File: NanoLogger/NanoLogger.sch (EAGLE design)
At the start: 18 parts, among them IC1 TINY11S, U4 LIS331, X1 USB-MICROB

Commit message: Lots of fixes, added NanoLogger
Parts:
- removed BAT1: (no value), SparkFun:BATTERY20SMD
- removed JP2: (no value), SparkFun:M061X06-SMD_EDGE_FEMALE
- removed R1, R2: 68, SparkFun:RESISTOR0402-RES
- removed R4: 1.5k, SparkFun:RESISTOR0402-RES
- removed R7: 4.7k, SparkFun:RESISTOR0402-RES
- removed X1: USB-MICROB, SparkFun:USB-MICROB
- added BAT2: (no value), SparkFun:BATTERY12MM
- added CS, GND, MISO, MOSI, SCK, VCC: TPTP08R, testpad:TPTP08R
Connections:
- removed net N$13: IC1.(XTAL2)PB4, R1.1, R6.2
- removed net N$2: R2.2, X1.D+
- removed net N$8: R1.2, R4.1, X1.D-
- removed net N$9: IC1.(RESET)PB5, R7.1
- new net N$11: IC1.(XTAL2)PB4, U4.CS
- new net N$12: CS.TP, IC1.(RESET)PB5, R6.2, U4.INT1
- net GND: now also BAT2.-, GND.TP; no longer BAT1.-, JP2.5, X1.GND
- net N$4: no longer JP2.4, R2.1, U4.CS
- net N$5: now also SCK.TP; no longer JP2.3
- net N$6: now also MOSI.TP; no longer JP2.1, U4.INT1
- net N$7: now also MISO.TP; no longer JP2.2
- net VCC: now also BAT2.+, VCC.TP; no longer BAT1.+, JP2.6, R4.2, R7.2
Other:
- note added: "NanoLogger"
- note removed: "CoinLogger"
- note removed: "If it's an input, we can look for the accel interrupt for ultra low power mode."
- note removed: "It's also CS, so by default, the accel is selected, but Flash can also be selected if CS is driven low."
- note removed: "PB4: LED is on by default since that line is pulled up because of USB"
- moved on the sheet: R6

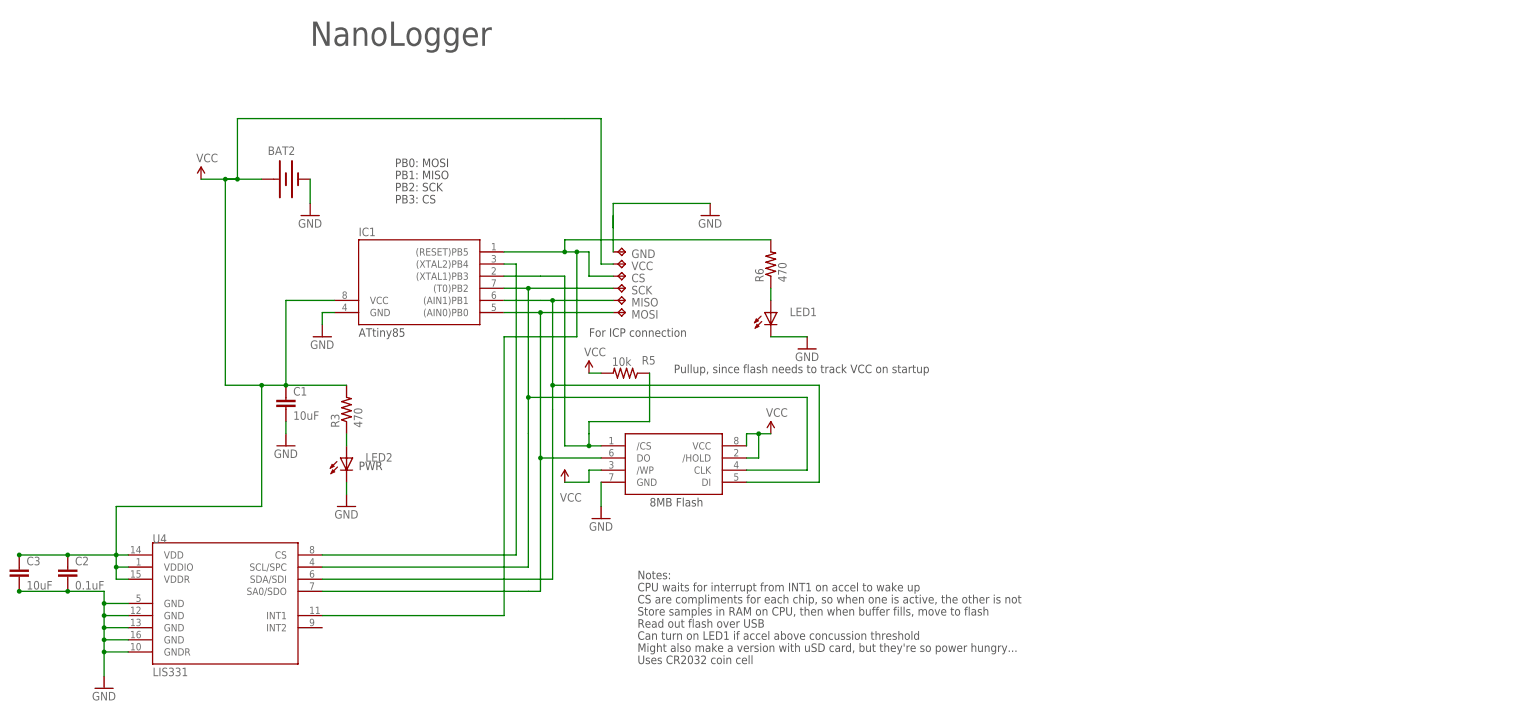
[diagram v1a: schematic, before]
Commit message: Updated and rerouted V1.1, early nanologger layout
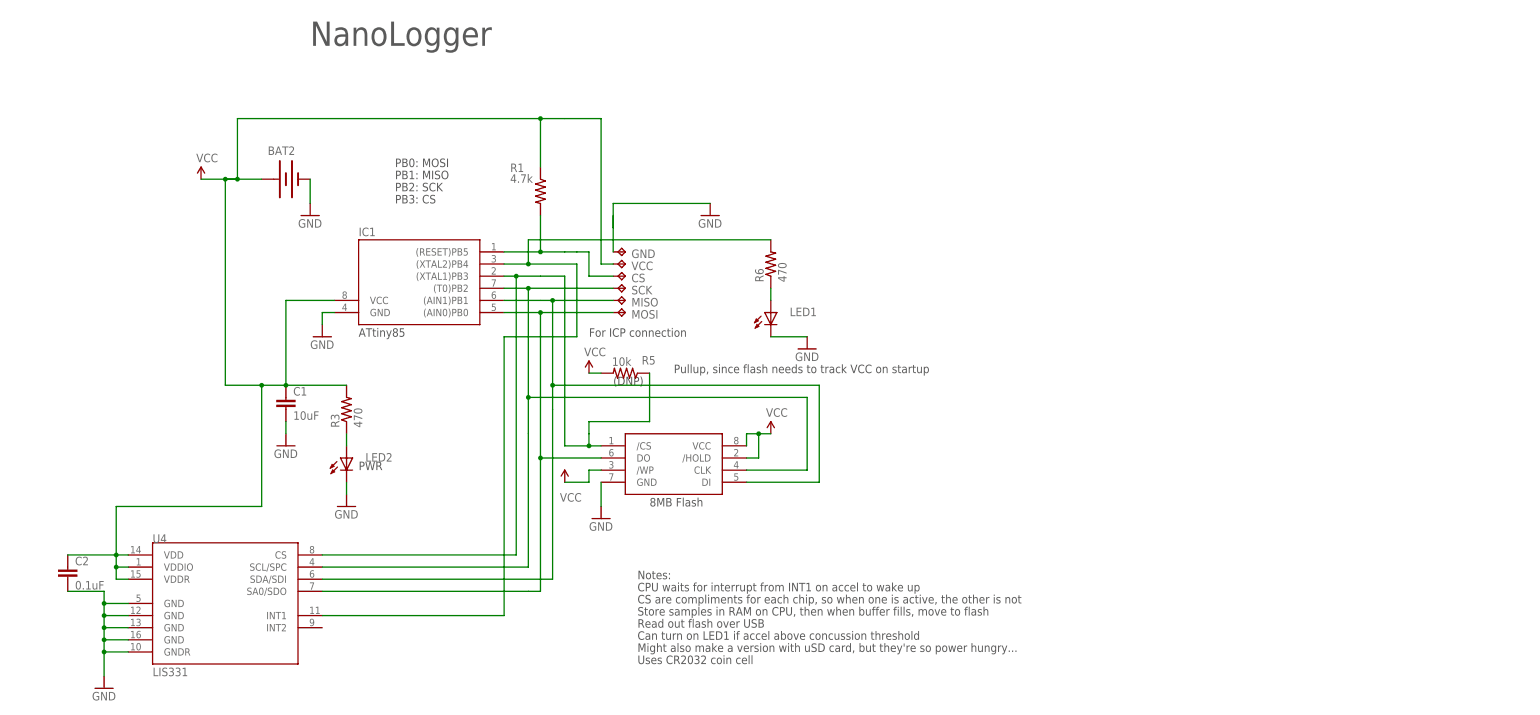
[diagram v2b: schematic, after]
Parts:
- removed C3: 10uF, SparkFun:CAP0402-CAP
- added R1: 4.7k, SparkFun:RESISTOR0402-RES
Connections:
- removed net N$4: IC1.(XTAL1)PB3, R5.1, U$1./CS
- new net N$2: CS.TP, IC1.(RESET)PB5, R1.2
- net GND: no longer C3.2
- net N$11: now also IC1.(XTAL1)PB3, R5.1, U$1./CS; no longer IC1.(XTAL2)PB4
- net N$12: now also IC1.(XTAL2)PB4; no longer CS.TP, IC1.(RESET)PB5
- net VCC: now also R1.1; no longer C3.1
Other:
- note added: "(DNP)"
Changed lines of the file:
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@@
 <part name="LED2" library="SparkFun" deviceset="LED" device="0603"/>
 <part name="C2" library="SparkFun" deviceset="CAP" device="0402-CAP" value="0.1uF"/>
-<part name="C3" library="SparkFun" deviceset="CAP" device="0402-CAP" value="10uF"/>
 <part name="U$1" library="W25Q80BV" deviceset="W25Q80BV" device=""/>
 <part name="GND4" library="supply1" deviceset="GND" device=""/>
@@
 <part name="MISO" library="testpad" deviceset="TP" device="TP08R"/>
 <part name="MOSI" library="testpad" deviceset="TP" device="TP08R"/>
+<part name="R1" library="SparkFun" deviceset="RESISTOR" device="0402-RES" value="4.7k"/>
 </parts>
 <sheets>
@@
 <text x="33.02" y="73.66" size="1.778" layer="97">PB2: SCK</text>
 <text x="33.02" y="71.12" size="1.778" layer="97">PB3: CS</text>
+<text x="78.74" y="33.02" size="1.778" layer="97">(DNP)</text>
 </plain>
 <instances>
@@
 </instance>
 <instance part="C2" gate="G$1" x="-35.56" y="-7.62"/>
-<instance part="C3" gate="G$1" x="-45.72" y="-7.62"/>
 <instance part="U$1" gate="G$1" x="78.74" y="10.16"/>
 <instance part="GND4" gate="1" x="76.2" y="5.08"/>
@@
 <attribute name="NAME" x="82.55" y="46.99" size="1.778" layer="95"/>
 <attribute name="TP_SIGNAL_NAME" x="80.01" y="46.99" size="1.778" layer="97" rot="R270"/>
+</instance>
+<instance part="R1" gate="G$1" x="63.5" y="73.66" smashed="yes" rot="R270">
+<attribute name="NAME" x="57.15" y="77.6986" size="1.778" layer="95"/>
+<attribute name="VALUE" x="57.15" y="75.438" size="1.778" layer="96"/>
 </instance>
 </instances>
@@
 <junction x="-27.94" y="-20.32"/>
 <junction x="-27.94" y="-22.86"/>
-<pinref part="C3" gate="G$1" pin="2"/>
 <pinref part="C2" gate="G$1" pin="2"/>
-<wire x1="-45.72" y1="-10.16" x2="-35.56" y2="-10.16" width="0.1524" layer="91"/>
 <wire x1="-35.56" y1="-10.16" x2="-27.94" y2="-10.16" width="0.1524" layer="91"/>
 <wire x1="-27.94" y1="-10.16" x2="-27.94" y2="-12.7" width="0.1524" layer="91"/>
 <junction x="-27.94" y="-12.7"/>
-<junction x="-35.56" y="-10.16"/>
-<junction x="-45.72" y="-10.16"/>
 </segment>
 <segment>
@@
 <pinref part="R3" gate="G$1" pin="1"/>
 <pinref part="LED2" gate="G$1" pin="A"/>
-</segment>
-</net>
-<net name="N$4" class="0">
-<segment>
-<pinref part="IC1" gate="G$1" pin="(XTAL1)PB3"/>
-<wire x1="55.88" y1="55.88" x2="63.5" y2="55.88" width="0.1524" layer="91"/>
-<wire x1="63.5" y1="55.88" x2="68.58" y2="55.88" width="0.1524" layer="91"/>
-<wire x1="68.58" y1="30.48" x2="68.58" y2="55.88" width="0.1524" layer="91"/>
-<wire x1="68.58" y1="30.48" x2="68.58" y2="20.32" width="0.1524" layer="91"/>
-<pinref part="U$1" gate="G$1" pin="/CS"/>
-<wire x1="68.58" y1="20.32" x2="73.66" y2="20.32" width="0.1524" layer="91"/>
-<pinref part="R5" gate="G$1" pin="1"/>
-<wire x1="73.66" y1="20.32" x2="76.2" y2="20.32" width="0.1524" layer="91"/>
-<wire x1="86.36" y1="35.56" x2="86.36" y2="25.4" width="0.1524" layer="91"/>
-<wire x1="86.36" y1="25.4" x2="73.66" y2="25.4" width="0.1524" layer="91"/>
-<wire x1="73.66" y1="25.4" x2="73.66" y2="22.86" width="0.1524" layer="91"/>
-<wire x1="73.66" y1="22.86" x2="73.66" y2="20.32" width="0.1524" layer="91"/>
-<junction x="73.66" y="20.32"/>
 </segment>
 </net>
@@
 <net name="N$11" class="0">
 <segment>
-<pinref part="IC1" gate="G$1" pin="(XTAL2)PB4"/>
-<wire x1="55.88" y1="58.42" x2="58.42" y2="58.42" width="0.1524" layer="91"/>
 <pinref part="U4" gate="G$1" pin="CS"/>
 <wire x1="17.78" y1="-2.54" x2="58.42" y2="-2.54" width="0.1524" layer="91"/>
-<wire x1="58.42" y1="-2.54" x2="58.42" y2="58.42" width="0.1524" layer="91"/>
+<pinref part="IC1" gate="G$1" pin="(XTAL1)PB3"/>
+<wire x1="55.88" y1="55.88" x2="58.42" y2="55.88" width="0.1524" layer="91"/>
+<wire x1="58.42" y1="55.88" x2="63.5" y2="55.88" width="0.1524" layer="91"/>
+<wire x1="63.5" y1="55.88" x2="68.58" y2="55.88" width="0.1524" layer="91"/>
+<wire x1="68.58" y1="30.48" x2="68.58" y2="55.88" width="0.1524" layer="91"/>
+<wire x1="68.58" y1="30.48" x2="68.58" y2="20.32" width="0.1524" layer="91"/>
+<pinref part="U$1" gate="G$1" pin="/CS"/>
+<wire x1="68.58" y1="20.32" x2="73.66" y2="20.32" width="0.1524" layer="91"/>
+<pinref part="R5" gate="G$1" pin="1"/>
+<wire x1="73.66" y1="20.32" x2="76.2" y2="20.32" width="0.1524" layer="91"/>
+<wire x1="86.36" y1="35.56" x2="86.36" y2="25.4" width="0.1524" layer="91"/>
+<wire x1="86.36" y1="25.4" x2="73.66" y2="25.4" width="0.1524" layer="91"/>
+<wire x1="73.66" y1="25.4" x2="73.66" y2="22.86" width="0.1524" layer="91"/>
+<wire x1="73.66" y1="22.86" x2="73.66" y2="20.32" width="0.1524" layer="91"/>
+<junction x="73.66" y="20.32"/>
+<wire x1="58.42" y1="-2.54" x2="58.42" y2="55.88" width="0.1524" layer="91"/>
+<junction x="58.42" y="55.88"/>
 </segment>
 </net>
@@
 <pinref part="R3" gate="G$1" pin="2"/>
 <pinref part="C1" gate="G$1" pin="1"/>
-<wire x1="68.58" y1="88.9" x2="0" y2="88.9" width="0.1524" layer="91"/>
+<wire x1="68.58" y1="88.9" x2="63.5" y2="88.9" width="0.1524" layer="91"/>
+<wire x1="63.5" y1="88.9" x2="0" y2="88.9" width="0.1524" layer="91"/>
 <wire x1="0" y1="88.9" x2="0" y2="76.2" width="0.1524" layer="91"/>
 <junction x="0" y="76.2"/>
-<pinref part="C3" gate="G$1" pin="1"/>
 <pinref part="C2" gate="G$1" pin="1"/>
-<wire x1="-45.72" y1="-2.54" x2="-35.56" y2="-2.54" width="0.1524" layer="91"/>
 <wire x1="-25.4" y1="-2.54" x2="-35.56" y2="-2.54" width="0.1524" layer="91"/>
 <junction x="-2.54" y="76.2"/>
-<junction x="-45.72" y="-2.54"/>
-<junction x="-35.56" y="-2.54"/>
 <junction x="5.08" y="33.02"/>
 <pinref part="BAT2" gate="G$1" pin="+"/>
@@
 <wire x1="76.2" y1="88.9" x2="68.58" y2="88.9" width="0.1524" layer="91"/>
 <pinref part="VCC" gate="G$1" pin="TP"/>
+<pinref part="R1" gate="G$1" pin="1"/>
+<wire x1="63.5" y1="78.74" x2="63.5" y2="88.9" width="0.1524" layer="91"/>
+<junction x="63.5" y="88.9"/>
 </segment>
 <segment>
@@
 <wire x1="17.78" y1="-15.24" x2="55.88" y2="-15.24" width="0.1524" layer="91"/>
 <wire x1="55.88" y1="-15.24" x2="55.88" y2="43.18" width="0.1524" layer="91"/>
+<wire x1="55.88" y1="43.18" x2="71.12" y2="43.18" width="0.1524" layer="91"/>
+<wire x1="71.12" y1="43.18" x2="71.12" y2="58.42" width="0.1524" layer="91"/>
+<pinref part="R6" gate="G$1" pin="2"/>
+<wire x1="111.76" y1="63.5" x2="60.96" y2="63.5" width="0.1524" layer="91"/>
+<wire x1="60.96" y1="63.5" x2="60.96" y2="58.42" width="0.1524" layer="91"/>
+<pinref part="IC1" gate="G$1" pin="(XTAL2)PB4"/>
+<wire x1="55.88" y1="58.42" x2="60.96" y2="58.42" width="0.1524" layer="91"/>
+<wire x1="71.12" y1="58.42" x2="60.96" y2="58.42" width="0.1524" layer="91"/>
+<junction x="60.96" y="58.42"/>
+</segment>
+</net>
+<net name="N$2" class="0">
+<segment>
+<pinref part="CS" gate="G$1" pin="TP"/>
+<wire x1="73.66" y1="55.88" x2="78.74" y2="55.88" width="0.1524" layer="91"/>
+<wire x1="73.66" y1="60.96" x2="73.66" y2="55.88" width="0.1524" layer="91"/>
+<wire x1="71.12" y1="60.96" x2="73.66" y2="60.96" width="0.1524" layer="91"/>
+<wire x1="68.58" y1="60.96" x2="71.12" y2="60.96" width="0.1524" layer="91"/>
 <pinref part="IC1" gate="G$1" pin="(RESET)PB5"/>
-<wire x1="55.88" y1="60.96" x2="68.58" y2="60.96" width="0.1524" layer="91"/>
-<wire x1="68.58" y1="60.96" x2="71.12" y2="60.96" width="0.1524" layer="91"/>
-<wire x1="68.58" y1="60.96" x2="68.58" y2="63.5" width="0.1524" layer="91"/>
-<wire x1="68.58" y1="63.5" x2="111.76" y2="63.5" width="0.1524" layer="91"/>
-<junction x="68.58" y="60.96"/>
-<pinref part="R6" gate="G$1" pin="2"/>
-<wire x1="55.88" y1="43.18" x2="71.12" y2="43.18" width="0.1524" layer="91"/>
-<wire x1="71.12" y1="43.18" x2="71.12" y2="60.96" width="0.1524" layer="91"/>
-<wire x1="71.12" y1="60.96" x2="73.66" y2="60.96" width="0.1524" layer="91"/>
-<wire x1="73.66" y1="60.96" x2="73.66" y2="55.88" width="0.1524" layer="91"/>
-<wire x1="73.66" y1="55.88" x2="78.74" y2="55.88" width="0.1524" layer="91"/>
-<junction x="71.12" y="60.96"/>
-<pinref part="CS" gate="G$1" pin="TP"/>
-</segment>
-</net>
+<wire x1="55.88" y1="60.96" x2="63.5" y2="60.96" width="0.1524" layer="91"/>
+<pinref part="R1" gate="G$1" pin="2"/>
+<wire x1="63.5" y1="60.96" x2="68.58" y2="60.96" width="0.1524" layer="91"/>
+<wire x1="63.5" y1="68.58" x2="63.5" y2="60.96" width="0.1524" layer="91"/>
+<junction x="63.5" y="60.96"/>
+</segment>
+</net>
